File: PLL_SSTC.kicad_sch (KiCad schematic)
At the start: 94 parts, among them J1 Conn_01x01_Socket, J2 Conn_01x01_Socket, J3 Conn_01x01_Socket, J4 Conn_01x01_Socket, J5 Conn_01x02_Socket, J6 Conn_01x02_Socket, J7 Conn_01x02_Socket, Q1 FDS4559, Q2 FDS4559, Q3 IRFP460PBF, Q4 IRFP460PBF, Q5 IRFP460PBF, Q6 IRFP460PBF, SW1 SW_SPST, U1 CD4046BE, U2 74HC74, U3 74HC14N, U4 ATtiny85-20P, U5 74HC08N, U6 MAX809SEUR_T10T, U8 LM7805_TO220

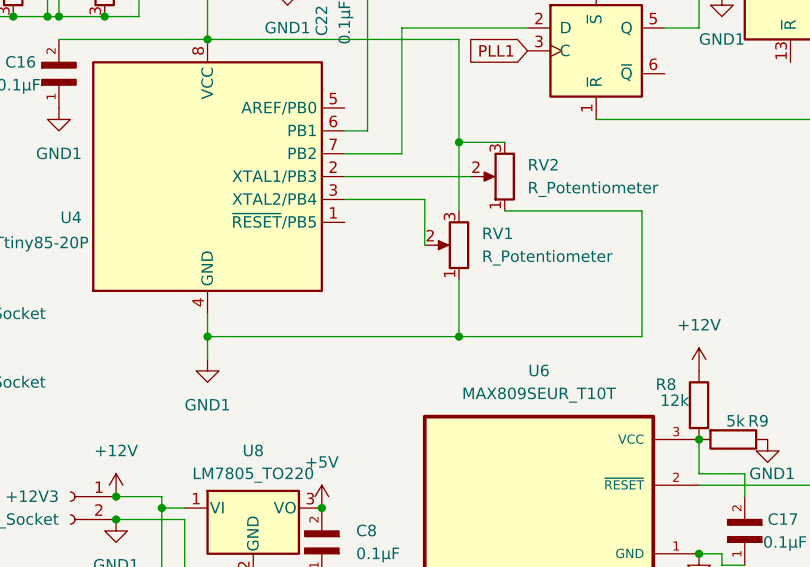
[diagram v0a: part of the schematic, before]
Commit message: fixed power connections and added mounting holes
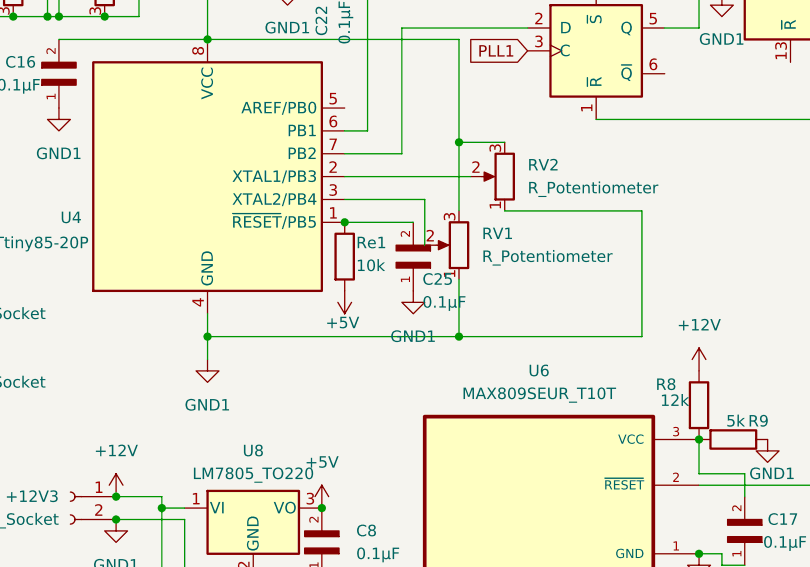
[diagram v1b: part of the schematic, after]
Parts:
- added C25: 0.1µF, Capacitor_SMD:C_0603_1608Metric_Pad1.08x0.95mm_HandSolder, symbol SR201C104KART:SR201C104KART
- added Re1: 10k, Resistor_THT:R_Axial_DIN0204_L3.6mm_D1.6mm_P1.90mm_Vertical, symbol Device:R
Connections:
- net +5V: now also Re1.2
- net GND1: now also C25.1
- net at U4.1 (~{RESET}/PB5): now also C25.2, Re1.1
